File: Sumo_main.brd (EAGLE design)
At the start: 70 x 24.5 mm, 41 parts, among them IC1 TL331, J2 MICRO_USB, T1 0603-PHOTO-TRANS, T2 0603-PHOTO-TRANS, U1 ATMEGA8U2AU, U2 SN65HVD3082, U3 LM339D, X1 MICROMATCH-12, X2 RS485, Y1 16MHz

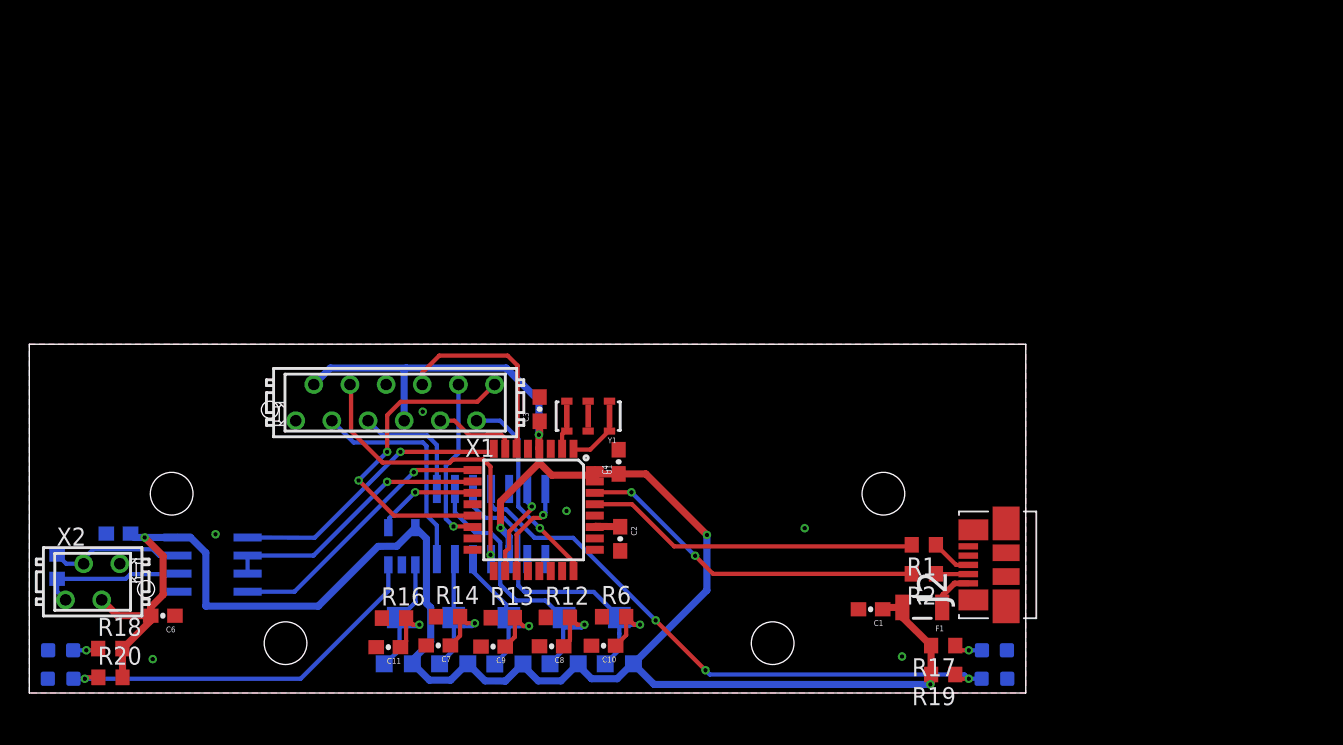
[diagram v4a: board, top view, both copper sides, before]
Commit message: Adjust GND plate to actual board shape
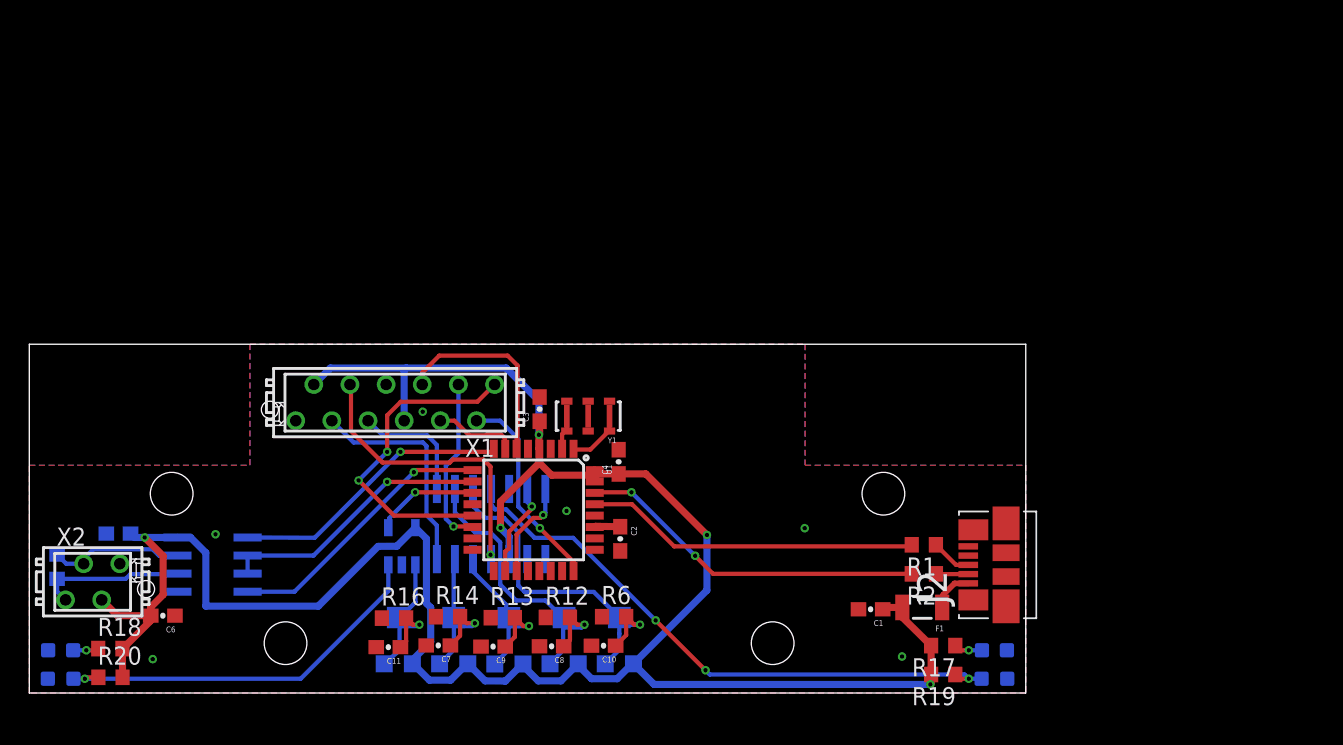
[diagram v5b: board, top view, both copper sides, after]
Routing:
- added copper zone on layer 16, net N$4
- added copper zone on layer 1, net N$8
- removed copper zone on layer 1, net GND
- removed copper zone on layer 16, net GND
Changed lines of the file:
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@@
 <contactref element="C8" pad="2"/>
 <contactref element="J2" pad="5"/>
-<polygon width="0.3" layer="1">
-<vertex x="0" y="24.5"/>
-<vertex x="70" y="24.5"/>
-<vertex x="70" y="0"/>
-<vertex x="0" y="0"/>
-</polygon>
-<polygon width="0.3" layer="16">
-<vertex x="0" y="24.5"/>
-<vertex x="70" y="24.5"/>
-<vertex x="70" y="0"/>
-<vertex x="0" y="0"/>
-</polygon>
 <contactref element="C5" pad="1"/>
 <contactref element="R6" pad="1"/>
@@
 <via x="8.67" y="2.38" extent="1-16" drill="0.3"/>
 <via x="61.31" y="2.56" extent="1-16" drill="0.3"/>
-<wire x1="27.64" y1="19.76" x2="25.065" y2="21.67" width="0" layer="19" extent="1-1"/>
-<wire x1="26.17" y1="9.004" x2="24.77" y2="5.26" width="0" layer="19" extent="1-16"/>
-<wire x1="33.71" y1="14.3338" x2="36.63" y2="17.1526" width="0" layer="19" extent="1-16"/>
 <via x="13.08" y="11.15" extent="1-16" drill="0.3"/>
 <via x="54.47" y="11.58" extent="1-16" drill="0.3"/>
+<wire x1="68.677" y1="3" x2="65.96" y2="10.3" width="0" layer="19" extent="1-16"/>
+<wire x1="68.7" y1="1" x2="68.677" y2="3" width="0" layer="19" extent="16-16"/>
+<wire x1="61.31" y1="2.56" x2="68.677" y2="3" width="0" layer="19" extent="16-16"/>
+<wire x1="58.25" y1="5.88" x2="61.31" y2="2.56" width="0" layer="19" extent="1-1"/>
+<wire x1="54.47" y1="11.58" x2="58.25" y2="5.88" width="0" layer="19" extent="1-1"/>
+<wire x1="41.51" y1="9.98" x2="54.47" y2="11.58" width="0" layer="19" extent="1-1"/>
+<wire x1="39.7226" y1="12.46" x2="41.51" y2="9.98" width="0" layer="19" extent="1-1"/>
+<wire x1="37.74" y1="12.79" x2="39.7226" y2="12.46" width="0" layer="19" extent="1-1"/>
+<wire x1="33.71" y1="14.3338" x2="37.74" y2="12.79" width="0" layer="19" extent="16-16"/>
+<wire x1="36.63" y1="17.1526" x2="33.71" y2="14.3338" width="0" layer="19" extent="1-16"/>
+<wire x1="39.26" y1="19.45" x2="36.63" y2="17.1526" width="0" layer="19" extent="1-1"/>
+<wire x1="41.4" y1="17.09" x2="39.26" y2="19.45" width="0" layer="19" extent="1-1"/>
+<wire x1="35.85" y1="20.79" x2="39.26" y2="19.45" width="0" layer="19" extent="1-1"/>
+<wire x1="40.23" y1="5.36" x2="41.51" y2="9.98" width="0" layer="19" extent="1-1"/>
+<wire x1="39.49" y1="3.32" x2="40.23" y2="5.36" width="0" layer="19" extent="1-1"/>
+<wire x1="35.84" y1="3.28" x2="39.49" y2="3.32" width="0" layer="19" extent="1-1"/>
+<wire x1="36.28" y1="5.31" x2="35.84" y2="3.28" width="0" layer="19" extent="1-1"/>
+<wire x1="32.41" y1="5.29" x2="36.28" y2="5.31" width="0" layer="19" extent="1-1"/>
+<wire x1="31.73" y1="3.26" x2="32.41" y2="5.29" width="0" layer="19" extent="1-1"/>
+<wire x1="28.56" y1="5.36" x2="31.73" y2="3.26" width="0" layer="19" extent="1-1"/>
+<wire x1="27.88" y1="3.34" x2="28.56" y2="5.36" width="0" layer="19" extent="1-1"/>
+<wire x1="24.37" y1="3.22" x2="27.88" y2="3.34" width="0" layer="19" extent="1-1"/>
+<wire x1="24.77" y1="5.26" x2="24.37" y2="3.22" width="0" layer="19" extent="1-1"/>
+<wire x1="26.17" y1="9.004" x2="24.77" y2="5.26" width="0" layer="19" extent="1-16"/>
+<wire x1="27.64" y1="19.76" x2="33.71" y2="14.3338" width="0" layer="19" extent="16-16"/>
+<wire x1="25.065" y1="21.67" x2="27.64" y2="19.76" width="0" layer="19" extent="1-1"/>
+<wire x1="18.715" y1="19.13" x2="25.065" y2="21.67" width="0" layer="19" extent="1-1"/>
+<wire x1="13.08" y1="11.15" x2="18.715" y2="19.13" width="0" layer="19" extent="1-1"/>
+<wire x1="10.4062" y1="7.115" x2="13.08" y2="11.15" width="0" layer="19" extent="16-16"/>
+<wire x1="10.23" y1="5.43" x2="10.4062" y2="7.115" width="0" layer="19" extent="1-16"/>
+<wire x1="8.67" y1="2.38" x2="10.23" y2="5.43" width="0" layer="19" extent="1-1"/>
+<wire x1="6.355" y1="9.08" x2="10.4062" y2="7.115" width="0" layer="19" extent="16-16"/>
+<wire x1="5.41" y1="11.2" x2="6.355" y2="9.08" width="0" layer="19" extent="16-16"/>
+<wire x1="1.323" y1="3" x2="8.67" y2="2.38" width="0" layer="19" extent="16-16"/>
+<wire x1="1.3" y1="1" x2="1.323" y2="3" width="0" layer="19" extent="16-16"/>
 </signal>
 <signal name="N$5">
@@
 <wire x1="23.15" y1="14.93" x2="23.13" y2="14.93" width="0.3" layer="1"/>
 </signal>
+<signal name="N$4">
+<polygon width="0.4064" layer="16" isolate="0.254">
+<vertex x="0" y="0"/>
+<vertex x="0" y="16"/>
+<vertex x="15.5" y="16"/>
+<vertex x="15.5" y="24.5"/>
+<vertex x="54.5" y="24.5"/>
+<vertex x="54.5" y="16"/>
+<vertex x="70" y="16"/>
+<vertex x="70" y="0"/>
+</polygon>
+</signal>
+<signal name="N$8">
+<polygon width="0.4064" layer="1" isolate="0.254">
+<vertex x="0" y="0"/>
+<vertex x="0" y="16"/>
+<vertex x="15.5" y="16"/>
+<vertex x="15.5" y="24.5"/>
+<vertex x="54.5" y="24.5"/>
+<vertex x="54.5" y="16"/>
+<vertex x="70" y="16"/>
+<vertex x="70" y="0"/>
+</polygon>
+</signal>
 </signals>

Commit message: Mark correct PCB shape
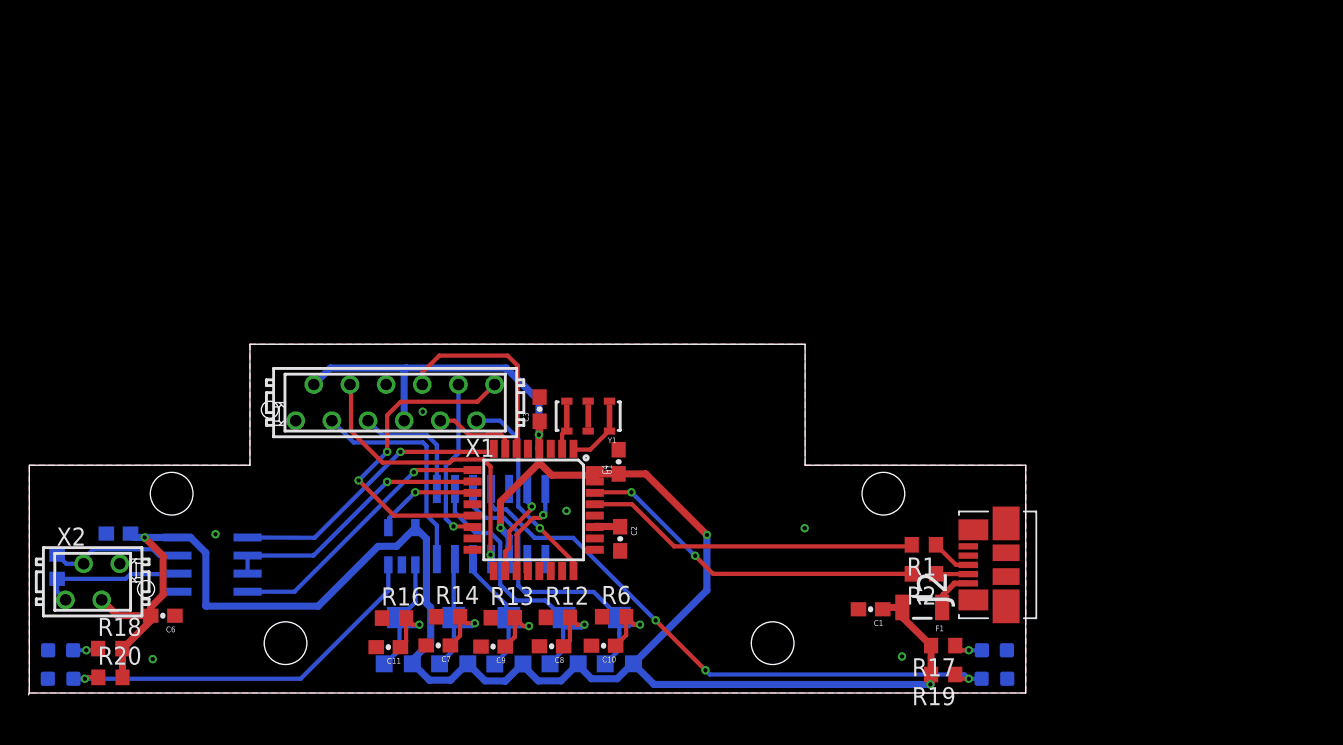
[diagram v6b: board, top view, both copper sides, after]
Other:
- board size 70 x 24.5 mm -> 70.1 x 24.6 mm
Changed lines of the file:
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@@
 <plain>
 <wire x1="0" y1="0" x2="70" y2="0" width="0" layer="20"/>
-<wire x1="70" y1="0" x2="70" y2="24.5" width="0" layer="20"/>
-<wire x1="70" y1="24.5" x2="0" y2="24.5" width="0" layer="20"/>
-<wire x1="0" y1="24.5" x2="0" y2="0" width="0" layer="20"/>
 <hole x="8.2" y="7.3" drill="1.2"/>
 <hole x="16.9" y="19.9" drill="1.2"/>
@@
 <hole x="10" y="14" drill="3"/>
 <hole x="60" y="14" drill="3"/>
+<wire x1="-0.06" y1="-0.13" x2="0" y2="0" width="0" layer="20"/>
+<wire x1="0" y1="0" x2="0" y2="16" width="0" layer="20"/>
+<wire x1="0" y1="16" x2="15.5" y2="16" width="0" layer="20"/>
+<wire x1="15.5" y1="16" x2="15.5" y2="24.5" width="0" layer="20"/>
+<wire x1="15.5" y1="24.5" x2="54.5" y2="24.5" width="0" layer="20"/>
+<wire x1="54.5" y1="24.5" x2="54.5" y2="16" width="0" layer="20"/>
+<wire x1="54.5" y1="16" x2="70" y2="16" width="0" layer="20"/>
+<wire x1="70" y1="16" x2="70" y2="0" width="0" layer="20"/>
 </plain>
 <attributes>

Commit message: Final modifications before test order
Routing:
- net COMP_OUT2: track 0.00 -> 8.42 mm, vias 0 -> 1
- net COMP_OUT1: track 0.00 -> 3.48 mm, vias 0 -> 1
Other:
- board text added: "Control"
- board text added: "IR"
- board text added: "Motors"
- board text added: "Sensors"

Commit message: Update main board and schematic
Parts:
- removed D3, D4: IR LED, SparkFun-LED:LED-0603
- removed R17, R18: 1K, resistor:R0603
- removed R19, R20: 47K, resistor:R0603
- removed T1, T2: 0603-PHOTO-TRANS, Phototransistor 0603:PHOTOTRANSISTOR
- added R21, R7: 1K, resistor:R0603
- added R4, R5: 47K, resistor:R0603
- added U$1, U$2: QRE1113GR, personales:4LEADSMD
- moved C2 0.21 mm to (41.5, 10.6)
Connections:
- removed net N$15: D3.A, R17.1
- removed net N$18: D4.A, R18.1
- new net N$4: R21.1, U$1.A
- new net N$8: R7.1, U$2.A
- net GND: now also J2.M1, J2.M2, J2.M3, J2.M4, J2.M5, J2.M6, J2.P$5, U$1.E, U$1.K, U$2.E, U$2.K; no longer D3.C, D4.C, J2.5, T1.EMITTER, T2.EMITTER
- net LN1: now also R4.1, U$1.C; no longer R19.1, T1.COLLECTOR
- net LN2: now also R5.1, U$2.C; no longer R20.1, T2.COLLECTOR
- net N$1: now also J2.P$3; no longer J2.3
- net N$2: now also J2.P$2; no longer J2.2
- net N$3: now also J2.P$1; no longer J2.1
- net VCC: now also R21.2, R4.2, R5.2, R7.2; no longer R17.2, R18.2, R19.2, R20.2
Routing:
- net GND: track 0.00 -> 15.3 mm, vias 6 -> 13
- net N$4: track 0.00 -> 5.66 mm, vias 0 -> 1
- net LN2: track 27.5 -> 30.2 mm
- net N$8: track 0.00 -> 2.32 mm, vias 0 -> 1
- net N$15: track 2.02 -> 0.00 mm, vias 1 -> 0
- net N$18: track 1.82 -> 0.00 mm, vias 1 -> 0
- net LN1: track 41.8 -> 40.3 mm
- net VCC: track 162.3 -> 161.0 mm
- net RESET: track 14.8 -> 16.0 mm
- added copper zone on layer 1, net GND
- added copper zone on layer 16, net GND
- removed copper zone on layer 16, net N$4
- removed copper zone on layer 1, net N$8
